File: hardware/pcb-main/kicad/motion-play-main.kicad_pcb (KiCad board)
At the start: 4 copper layers, 35.8 x 82.6 mm, 52 parts, among them J10 Conn_01x02, J3 LED_Strip, J4 Conn_01x03, J5 Conn_01x03, J6 Conn_01x03, J7 Conn_01x03, J8 Conn_01x03, J9 Conn_01x03, U2 T-Display-S3, U3 TCA9548APWR, U4 AMS1117-3.3

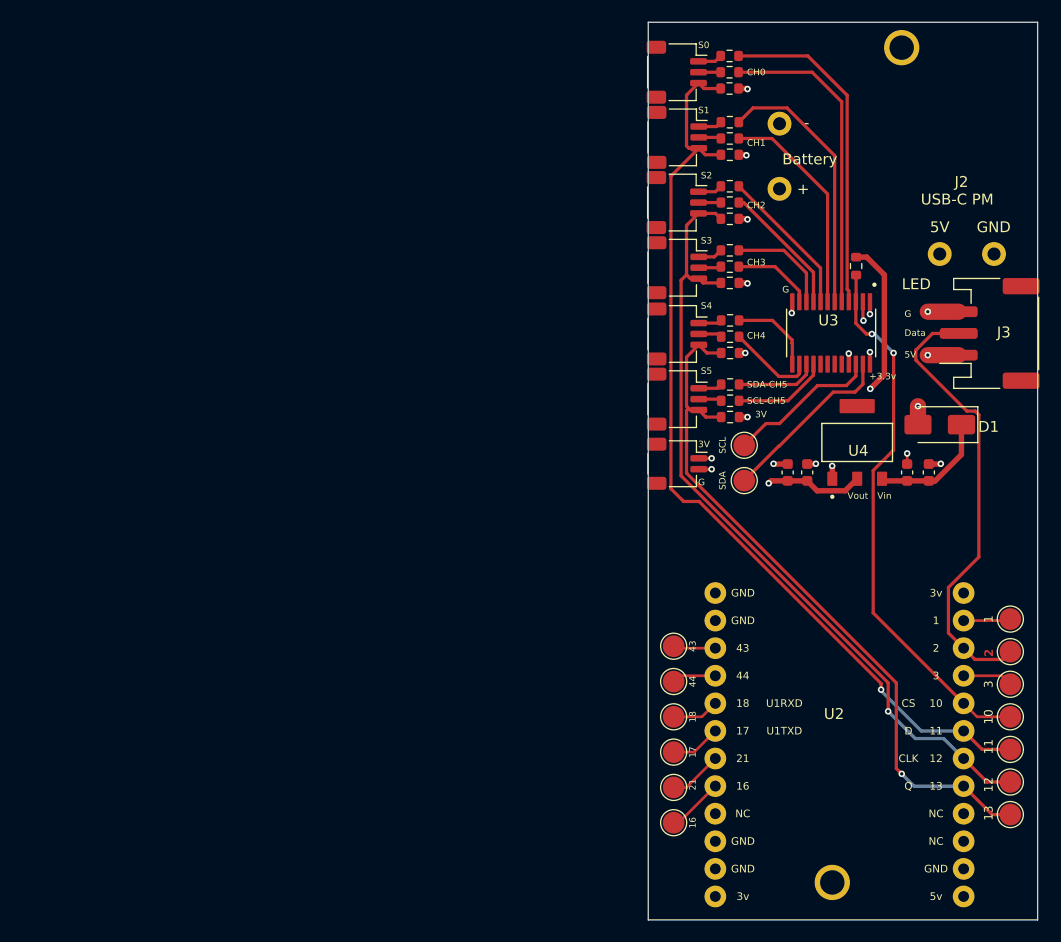
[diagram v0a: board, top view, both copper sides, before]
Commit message: Finished sensor redesign
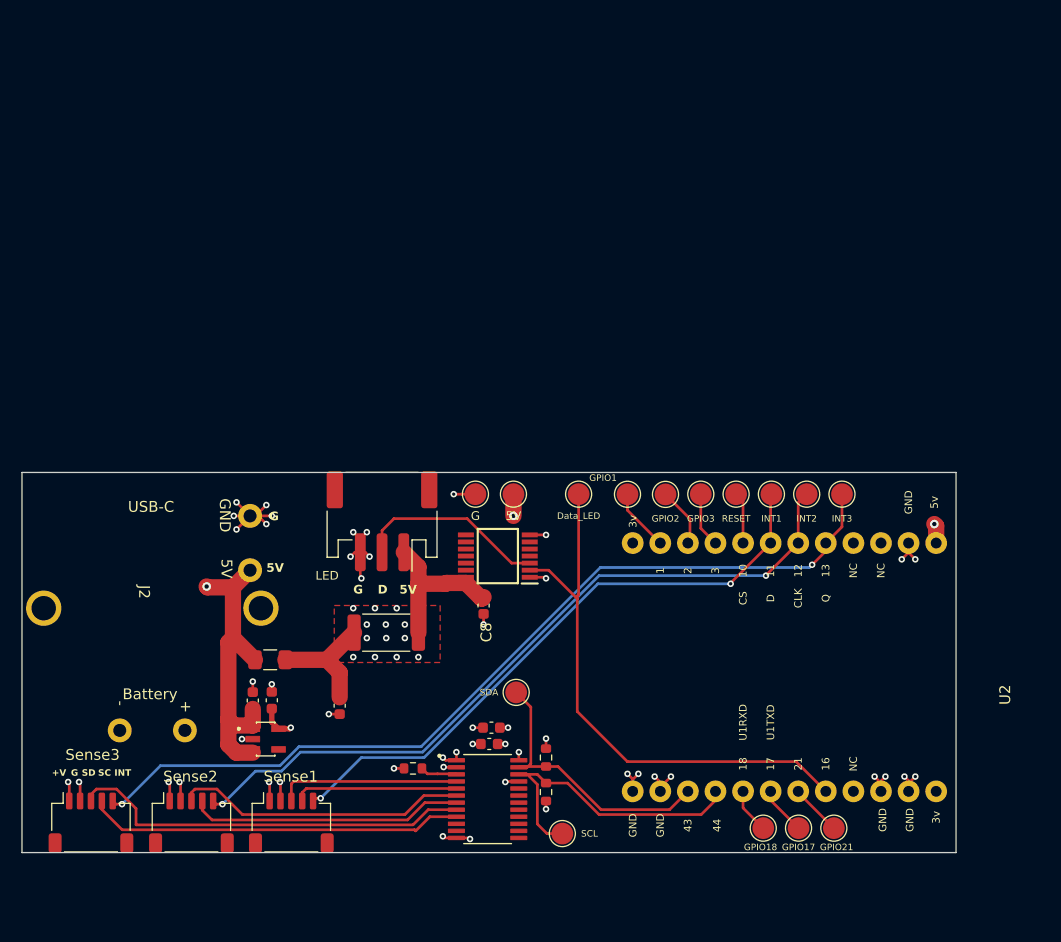
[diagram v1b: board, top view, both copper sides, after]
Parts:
- removed 1, 10, 11, 12, 13, 16, 17, 18, 2, 21, 3, 43, 44, SCL, SDA: TestPoint, TestPoint:TestPoint_Pad_D2.0mm
- removed ?: , 
- removed C3, C4: 0.1µF, Capacitor_SMD:C_0603_1608Metric
- removed D1: D_Schottky, Diode_SMD:D_SMA
- removed J10: Conn_01x02, Connector_JST:JST_SH_SM02B-SRSS-TB_1x02-1MP_P1.00mm_Horizontal
- removed J7, J8, J9: Conn_01x03, Connector_JST:JST_SH_SM03B-SRSS-TB_1x03-1MP_P1.00mm_Horizontal
- removed R10, R11, R12, R13, R14, R15, R16, R17, R18, R19, R20, R21: 100Ω, Resistor_SMD:R_0603_1608Metric
- removed R3, R4, R5, R7, R8, R9: 10kΩ, Resistor_SMD:R_0603_1608Metric
- removed U3: TCA9548APWR, TCA9548:SOP65P640X120-24N
- added C10: 10uF, Capacitor_SMD:C_0603_1608Metric, F.Cu at (121.2, 124.5)
- added C7: 100nF, Capacitor_SMD:C_0603_1608Metric, F.Cu at (107.2, 122.5)
- added C8: 10uF, Capacitor_SMD:C_0603_1608Metric, F.Cu at (120.5, 113.2)
- added C9: 100nF, Capacitor_SMD:C_0603_1608Metric, F.Cu at (121.0, 126.0)
- added F1: 3A, Fuse:Fuse_1206_3216Metric, F.Cu at (100.8, 118.2)
- added IC1: SN74AHCT125PWR, motion-play-footprints:SOP65P640X120-14N, F.Cu at (121.8, 108.7)
- added R27: 0.1R, Resistor_SMD:R_2512_6332Metric, F.Cu at (111.5, 115.8)
- added R28: 2.2kΩ, Resistor_SMD:R_0603_1608Metric, F.Cu at (126.2, 127.2)
- added R29: 2.2kΩ, Resistor_SMD:R_0603_1608Metric, F.Cu at (126.2, 130.4)
- added TPIO1: TestPoint, TestPoint:TestPoint_Pad_D2.0mm, F.Cu at (133.8, 103.0)
- added TPIO10: TestPoint, TestPoint:TestPoint_Pad_D2.0mm, F.Cu at (143.8, 103.0)
- added TPIO11: TestPoint, TestPoint:TestPoint_Pad_D2.0mm, F.Cu at (147.0, 103.0)
- added TPIO12: TestPoint, TestPoint:TestPoint_Pad_D2.0mm, F.Cu at (150.2, 103.0)
- added TPIO13: TestPoint, TestPoint:TestPoint_Pad_D2.0mm, F.Cu at (153.5, 103.0)
- added TPIO16: TestPoint, TestPoint:TestPoint_Pad_D2.0mm, F.Cu at (129.2, 103.0)
- added TPIO17: TestPoint, TestPoint:TestPoint_Pad_D2.0mm, F.Cu at (149.5, 133.8)
- added TPIO18: TestPoint, TestPoint:TestPoint_Pad_D2.0mm, F.Cu at (146.2, 133.8)
- added TPIO2: TestPoint, TestPoint:TestPoint_Pad_D2.0mm, F.Cu at (137.2, 103.0)
- added TPIO21: TestPoint, TestPoint:TestPoint_Pad_D2.0mm, F.Cu at (152.8, 133.8)
- added TPIO3: TestPoint, TestPoint:TestPoint_Pad_D2.0mm, F.Cu at (140.5, 103.0)
- added TPIO43: TestPoint, TestPoint:TestPoint_Pad_D2.0mm, F.Cu at (123.5, 121.2)
- added TPIO44: TestPoint, TestPoint:TestPoint_Pad_D2.0mm, F.Cu at (127.8, 134.2)
- added TP_5V1: TestPoint, TestPoint:TestPoint_Pad_D2.0mm, F.Cu at (123.2, 103.0)
- added TP_GND1: TestPoint, TestPoint:TestPoint_Pad_D2.0mm, F.Cu at (119.8, 103.0)
- added U1: AP2112K-3.3TRG1, motion-play-footprints:SOT95P285X140-5N, F.Cu at (100.4, 125.5)
- C1: value 10µF -> 1µF
- C2: value 22µF -> 2.2µF
- J2: value ~ -> DWEII Power Module; footprint Library:USBC_Power_Module -> motion-play-footprints:USBC_Power_Module
- J4, J5, J6: value Conn_01x03 -> Conn_01x05; footprint Connector_JST:JST_SH_SM03B-SRSS-TB_1x03-1MP_P1.00mm_Horizontal -> Connector_JST:JST_SH_SM05B-SRSS-TB_1x05-1MP_P1.00mm_Horizontal
- U2: footprint Library:T-Display-S3 -> motion-play-footprints:T-Display-S3
- U4: value AMS1117-3.3 -> TCA9548APWR; footprint AMS1117-3.3:SOT229P700X180-4N -> motion-play-footprints:SOP65P640X120-24N
- moved J6 78.5 mm to (84.3, 133.2), turned to 0 degrees
- moved J4 77.7 mm to (102.8, 133.2), turned to 0 degrees
- moved J5 77.3 mm to (93.6, 133.2), turned to 0 degrees
- moved J2 74.0 mm to (100.0, 101.0), turned to -90 degrees
- moved C1 63.8 mm to (99.2, 122.0), turned to -90 degrees
- moved R6 61.7 mm to (114.0, 128.2), turned to 180 degrees
- moved J3 58.6 mm to (111.2, 105.5), turned to 180 degrees
- moved C2 51.9 mm to (101.0, 122.0), turned to -90 degrees
- moved U4 47.3 mm to (120.9, 131.1), turned to 0 degrees
- moved U2 37.7 mm to (167.2, 107.5), turned to 90 degrees
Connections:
- C1 pad 1: Net-(D1-K) -> GND
- C1 pad 2: /GND -> +5V
- C2 pad 1: /+3.3V -> GND
- C2 pad 2: /GND -> +3.3V
- J2 pad 1: /GND -> GND
- J2 pad 2: /+5V -> +5V
- J4 pad 1: Net-(J4-Pin_1) -> +3.3V
- J4 pad 2: Net-(J4-Pin_2) -> GND
- J4 pad 3: Net-(J4-Pin_3) -> /TCA9548A_Subsystem/CH0_SDA
- J5 pad 1: Net-(J5-Pin_1) -> +3.3V
- J5 pad 2: Net-(J5-Pin_2) -> GND
- J5 pad 3: Net-(J4-Pin_3) -> /TCA9548A_Subsystem/CH1_SDA
- J6 pad 1: Net-(J6-Pin_1) -> +3.3V
- J6 pad 2: Net-(J6-Pin_2) -> GND
- J6 pad 3: Net-(J6-Pin_3) -> /TCA9548A_Subsystem/CH2_SDA
- R6 pad 1: Net-(U2-10) -> /TCA9548A_Subsystem/TCA_RESET
- R6 pad 2: /+3.3V -> +3.3V
- U2 pad 1: Net-(3V2-Pad1) -> unconnected-(U2-3v-Pad1)
- U2 pad 11: /GND -> GND
- U2 pad 12: /+5V -> +5V
- U2 pad 13: /GND -> GND
- U2 pad 14: /GND -> GND
- U2 pad 15: /SDA -> /I2C_SDA
- U2 pad 16: /SCL -> /I2C_SCL
- U2 pad 20: Net-(U2-16) -> /LED Controller/DATA_IN
- U2 pad 22: /GND -> GND
- U2 pad 23: /GND -> GND
- U2 pad 24: Net-(3V1-Pad1) -> unconnected-(U2-3v-Pad24)
- U2 pad 3: Net-(J3-Pin_2) -> Net-(U2-2)
- U2 pad 5: Net-(U2-10) -> /TCA9548A_Subsystem/TCA_RESET
- U2 pad 6: Net-(J4-Pin_3) -> /INT1
- U2 pad 7: Net-(J6-Pin_3) -> /INT2
- U2 pad 8: Net-(J8-Pin_3) -> /INT3
- U4 pad 1: /GND -> GND
- U4 pad 2: /+3.3V -> GND
- U4 pad 3: Net-(D1-K) -> /TCA9548A_Subsystem/TCA_RESET
- U4 pad 4: (no net) -> /TCA9548A_Subsystem/CH0_SDA
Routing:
- net Net-(J4-Pin_3): track 86.0 -> 0.00 mm, vias 1 -> 0
- net /INT3: track 0.00 -> 81.3 mm, vias 0 -> 2
- net Net-(J6-Pin_3): track 74.1 -> 0.00 mm, vias 1 -> 0
- net /INT2: track 0.00 -> 69.0 mm, vias 0 -> 2
- net Net-(J8-Pin_3): track 65.6 -> 0.00 mm, vias 1 -> 0
- net GND: track 0.00 -> 60.2 mm, vias 0 -> 53
- net /INT1: track 0.00 -> 57.0 mm, vias 0 -> 2
- net /LED Controller/DATA_IN: track 0.00 -> 51.5 mm
- net Net-(U2-10): track 50.4 -> 0.00 mm, vias 2 -> 0
- net Net-(J3-Pin_2): track 41.6 -> 0.00 mm
- net /TCA9548A_Subsystem/CH2_SDA: track 0.00 -> 37.3 mm
- net /TCA9548A_Subsystem/CH2_SCL: track 0.00 -> 34.8 mm
- net +5V: track 0.00 -> 34.6 mm, vias 0 -> 3
- net Net-(U3-SD0): track 30.6 -> 0.00 mm
- net /+3.3V: track 30.2 -> 0.00 mm, vias 10 -> 0
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- added copper zone on In2.Cu, net +3.3V
- added copper zone on In2.Cu, net +5V
- added copper zone on F.Cu, net GND
- added copper zone on In1.Cu, net GND
- removed copper zone on In2.Cu, net /+3.3V
- removed copper zone on In2.Cu, net /+5V
- removed copper zone on In1.Cu, net /GND
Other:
- board size 35.8 x 82.6 mm -> 86 x 35 mm
- board text added: "+V"
- board text added: "D"
- board text added: "INT"
- board text added: "SC"
- board text added: "SD"
- board text removed: "+3.3v"
- board text removed: "2"
- board text removed: "3V"
- board text removed: "CH0"
- board text removed: "CH1"
- board text removed: "CH2"
- board text removed: "CH3"
- board text removed: "CH4"
- board text removed: "Data"
- board text removed: "LED"
- board text removed: "S0"
- board text removed: "S1"
- board text removed: "S2"
- board text removed: "S3"
- board text removed: "S4"
- board text removed: "S5"
- board text removed: "SCL-CH5"
- board text removed: "SDA-CH5"
- board text removed: "Vin"
- board text removed: "Vout"
